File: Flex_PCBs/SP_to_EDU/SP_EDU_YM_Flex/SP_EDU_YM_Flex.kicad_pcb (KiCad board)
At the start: 2 copper layers, 59.5 x 55 mm, 2 parts, among them J1 Conn_01x08_Male, J2 Conn_01x08_Male

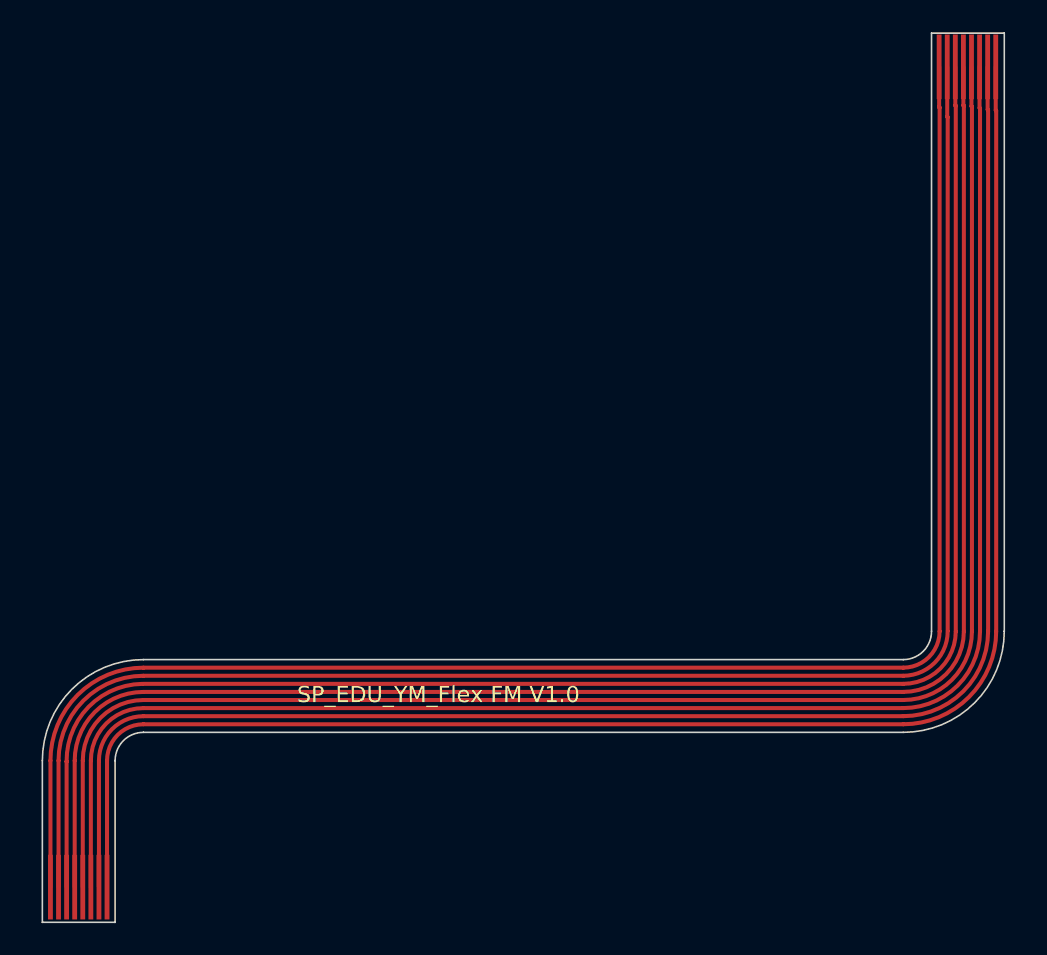
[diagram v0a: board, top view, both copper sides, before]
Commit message: replace ZF5S-*-01-T-WT and 2005280040 connectors with T1M-*-F-SH-L-FR connector
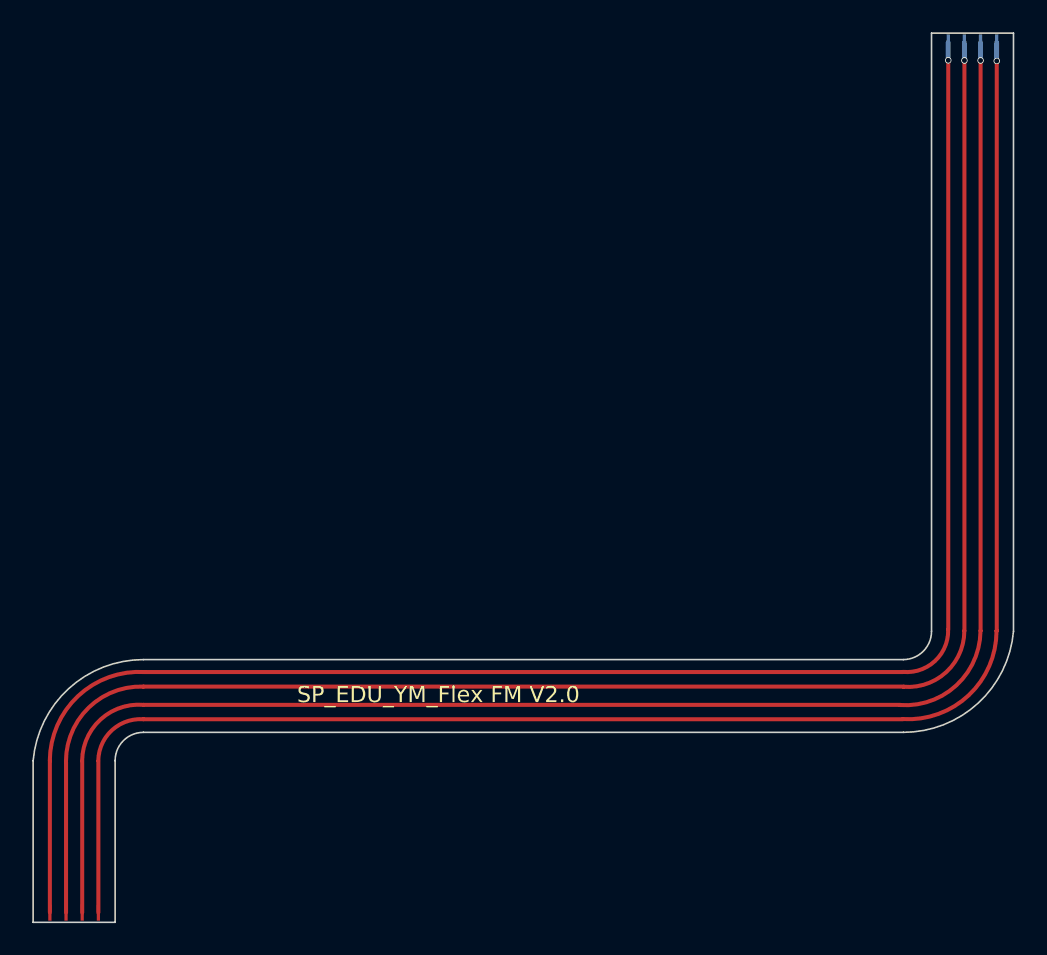
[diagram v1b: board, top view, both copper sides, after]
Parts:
- J1: value Conn_01x08_Male -> Conn_01x04_Pin; footprint STS_connector:flexpcb con. -> STS_connector:flexPCB_connector_edu_sensors_new; moved to B.Cu
- J2: value Conn_01x08_Male -> Conn_01x04_Pin; footprint STS_connector:flexpcb con. -> STS_connector:flexPCB_connector_edu_sensors_new
- moved J1 6.07 mm to (179.5, 55.1), turned to 180 degrees
- moved J2 5.48 mm to (120.0, 108.9), turned to 0 degrees
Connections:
- J1 pad 1: 8 -> 4
- J1 pad 2: 7 -> 3
- J1 pad 3: 6 -> 2
- J1 pad 4: 5 -> 1
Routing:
- net 5: track 89.8 -> 0.00 mm
- net 8: track 89.8 -> 0.00 mm
- net 7: track 89.7 -> 0.00 mm
- net 6: track 89.7 -> 0.00 mm
- net 4: track 89.8 -> 92.7 mm, vias 0 -> 1
- net 2: track 89.8 -> 92.7 mm, vias 0 -> 1
- net 3: track 89.8 -> 92.6 mm, vias 0 -> 1
- net 1: track 89.8 -> 92.6 mm, vias 0 -> 1
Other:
- board size 59.5 x 55 mm -> 60.6 x 55 mm
- board text added: "SP_EDU_YM_Flex FM V2.0"
- board text removed: "SP_EDU_YM_Flex FM V1.0"
